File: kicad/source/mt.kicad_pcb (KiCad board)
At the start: 4 copper layers, 166.4 x 127 mm, 138 parts, among them IC1 MCP73831T-2ACI_OT, IC10 SN74HC148NSR, IC11 SN74HC148NSR, IC2 BQ29728DSER, IC3 TLV74333PDBVR, IC4 TLV9152IDR, IC5 MSPM0G3507SPMR, IC6 IS62WV1288BLL-55QLI, IC7 DAC082S085CIMMX_NOPB, IC8 SN74HC148NSR, IC9 SN74HC148NSR, J1 694106301002, J10 Conn_01x02_Pin, J2 3557-2, J3 SJ1-3524N, J4 Conn_01x05_Pin, J5 Conn_01x09_Pin, J6 Conn_01x03_Pin, J7 Conn_01x03_Pin, J8 Conn_01x03_Pin, J9 Conn_01x02_Pin, Q1 CSD16406Q3, Q2 CSD16406Q3, U1 1043

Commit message: completed buttons arrangement
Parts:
- moved R36 397.7 mm to (168.3, 142.9)
- moved S22 397.7 mm to (163.2, 148.0)
- moved R39 393.8 mm to (208.3, 101.0)
- moved S25 393.8 mm to (203.2, 106.0)
- moved R37 390.3 mm to (175.9, 131.4)
- moved S23 390.3 mm to (170.8, 136.5)
- moved R38 383.8 mm to (183.5, 142.9)
- moved S24 383.8 mm to (178.4, 148.0)
- moved R32 368.6 mm to (137.8, 142.9)
- moved S18 368.6 mm to (132.7, 148.0)
- moved R33 360.6 mm to (145.4, 131.4)
- moved S19 360.6 mm to (140.3, 136.5)
- moved C24 357.6 mm to (147.3, 88.3)
- moved IC10 357.6 mm to (141.6, 92.7)
- moved R34 354.7 mm to (153.0, 142.9)
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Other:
- board size 166.4 x 127 mm -> 166.4 x 142.2 mm
- board text added: "Cancel"
- board text added: "Copy"
- board text added: "Cut"
- board text added: "Delete"
- board text added: "Down"
- board text added: "Edit/Play"
- board text added: "Editor Config"
- board text added: "End"
- board text added: "Enter"
- board text added: "Keyboard"
- board text added: "Left"
- board text added: "Load"
- board text added: "Matthew Nutt - Rice University - ELEC 327"
- board text added: "MicroTracker"
- board text added: "Note End"
- board text added: "Octave +"
- board text added: "Octave -"
- board text added: "Pattern/Song"
- board text added: "Rev. 1.0"
- board text added: "Right"
- board text added: "Save"
- board text added: "Select"
- board text added: "Skip"
- board text added: "Song Config"
- board text added: "Undo"
- board text added: "Up"

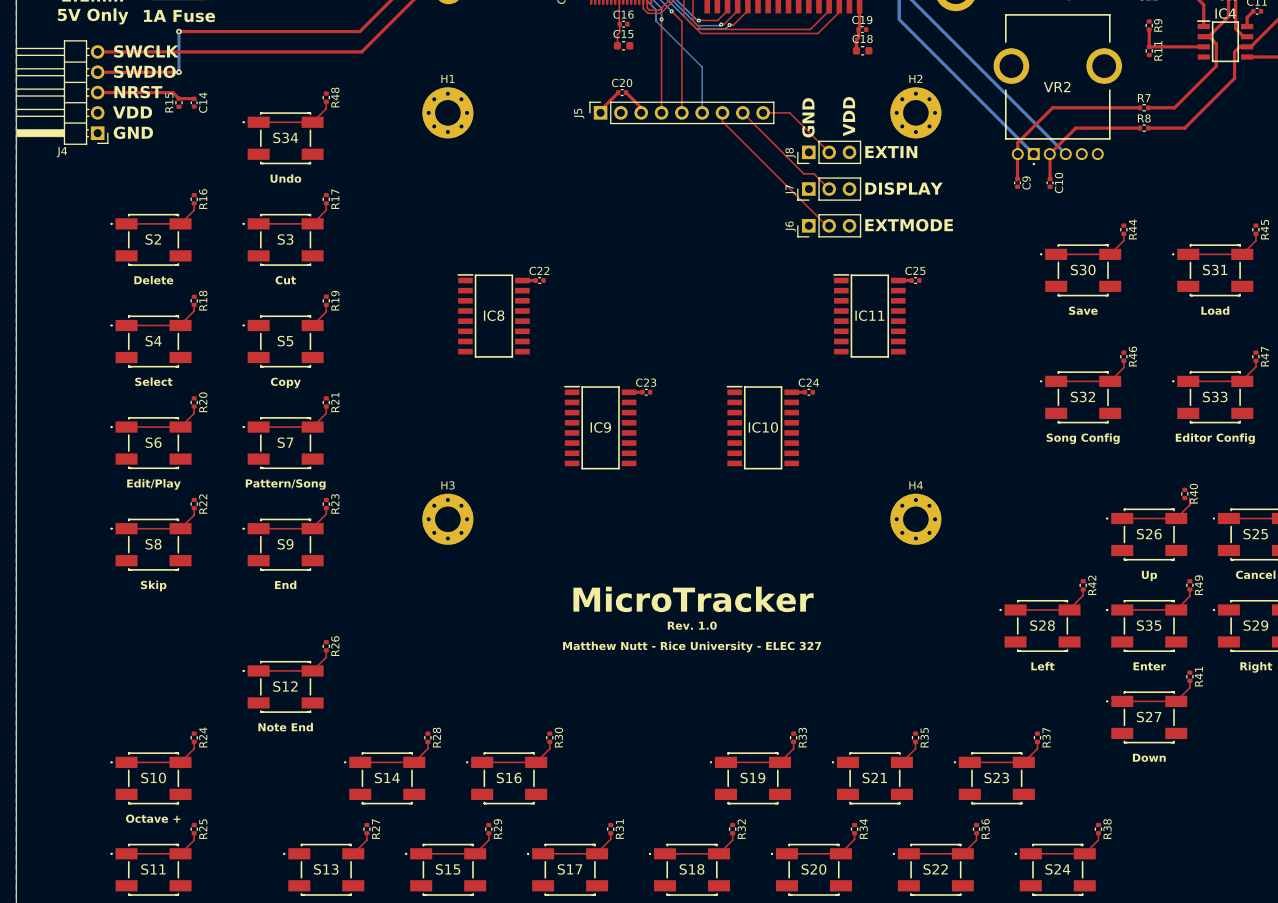
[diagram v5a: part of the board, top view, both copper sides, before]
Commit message: completed button-encoder routing
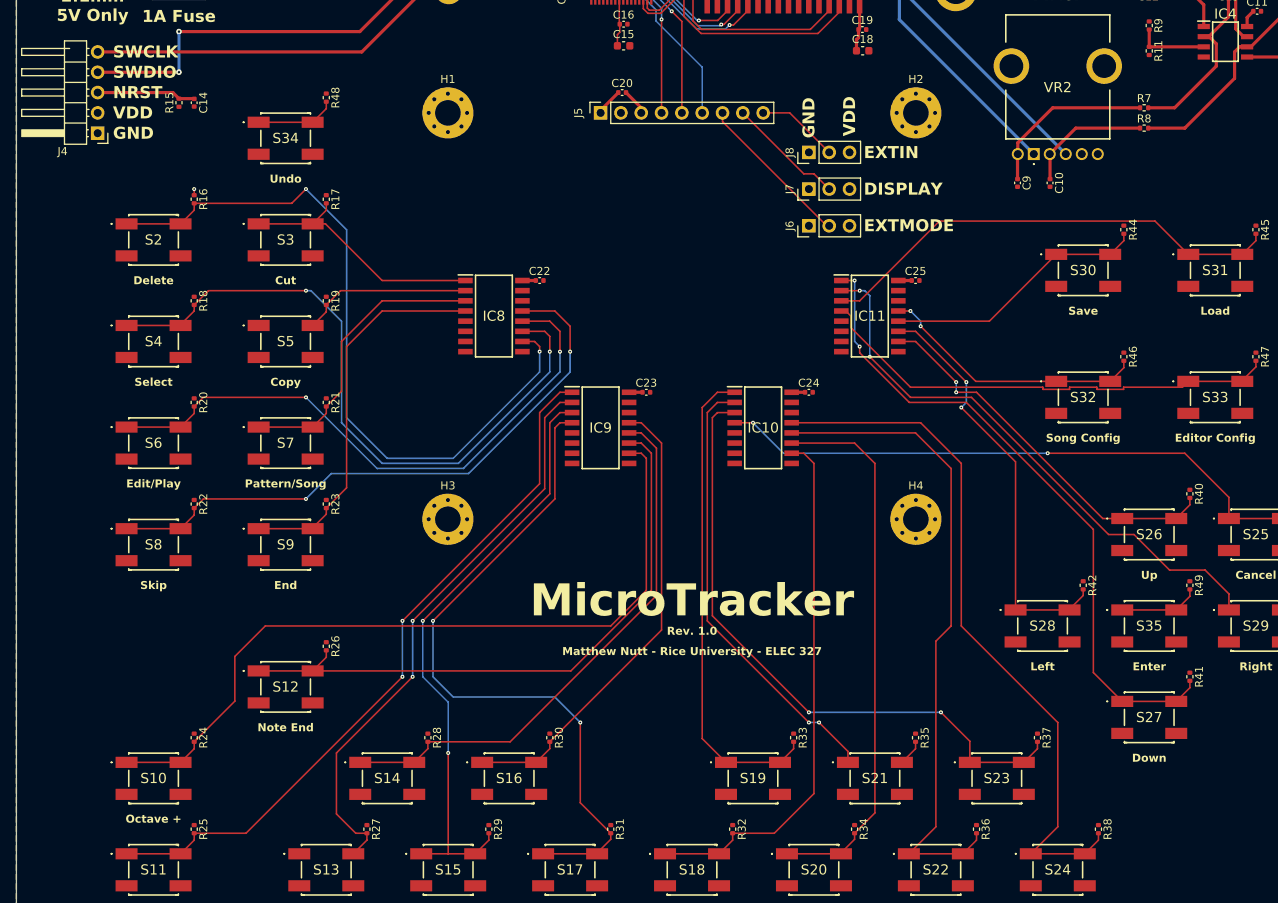
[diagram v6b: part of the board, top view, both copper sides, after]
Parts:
- moved R40 0.63 mm to (194.9, 101.0)
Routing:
- net Net-(IC9-0): track 10.0 -> 96.6 mm
- net Net-(IC8-0): track 10.0 -> 91.7 mm, vias 0 -> 2
- net Net-(IC9-4): track 10.0 -> 89.4 mm, vias 0 -> 2
- net Net-(IC10-3): track 10.0 -> 88.5 mm
- net Net-(IC9-7): track 10.0 -> 86.1 mm, vias 0 -> 2
- net Net-(IC8-1): track 10.0 -> 84.5 mm, vias 0 -> 2
- net Net-(IC11-4): track 10.0 -> 82.3 mm, vias 0 -> 2
- net Net-(IC10-2): track 10.0 -> 82.2 mm
- net Net-(IC11-5): track 3.28 -> 73.9 mm, vias 0 -> 2
- net Net-(IC9-5): track 3.28 -> 72.6 mm, vias 0 -> 2
- net Net-(IC10-6): track 10.0 -> 79.2 mm, vias 0 -> 2
- net Net-(IC10-7): track 10.0 -> 78.3 mm, vias 0 -> 2
- net Net-(IC9-1): track 10.0 -> 77.0 mm
- net Net-(IC8-3): track 10.0 -> 76.5 mm, vias 0 -> 2
- net Net-(IC8-2): track 10.0 -> 75.2 mm, vias 0 -> 2
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
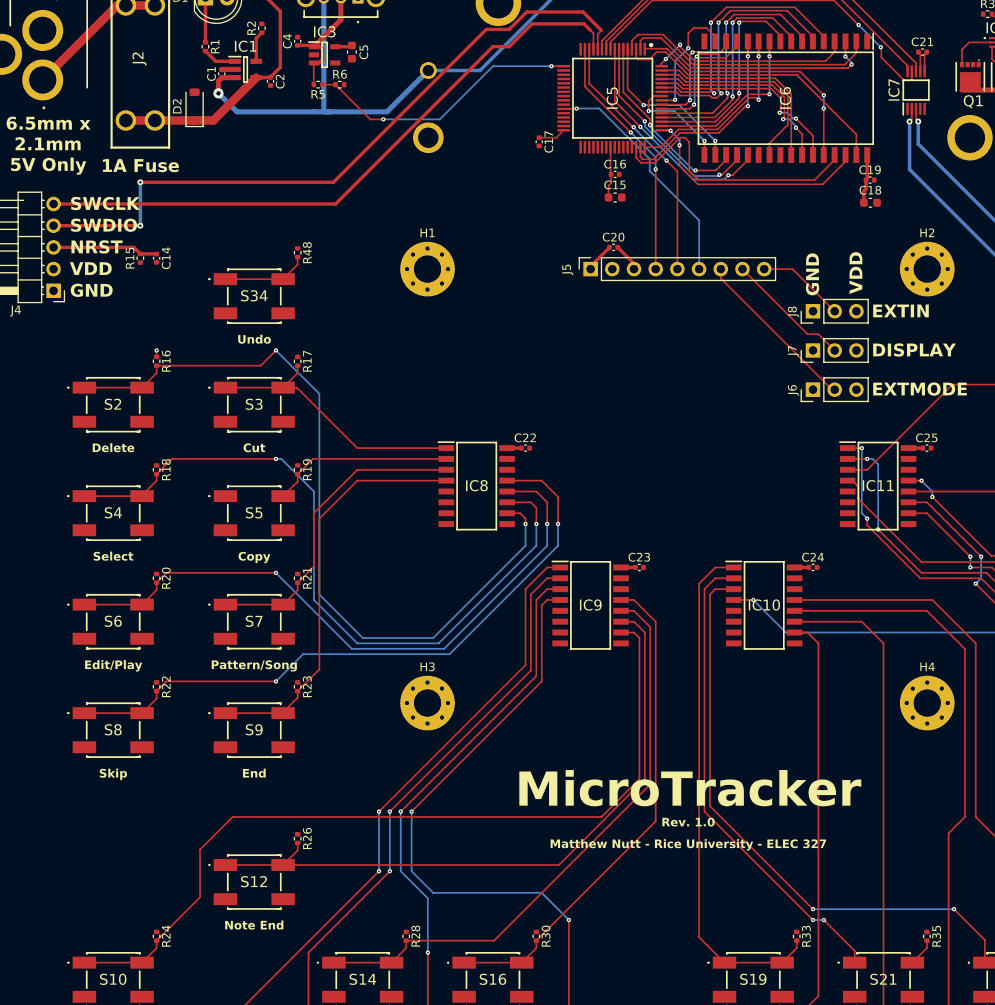
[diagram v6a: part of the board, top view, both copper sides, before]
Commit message: started encoder-microcontroller routing
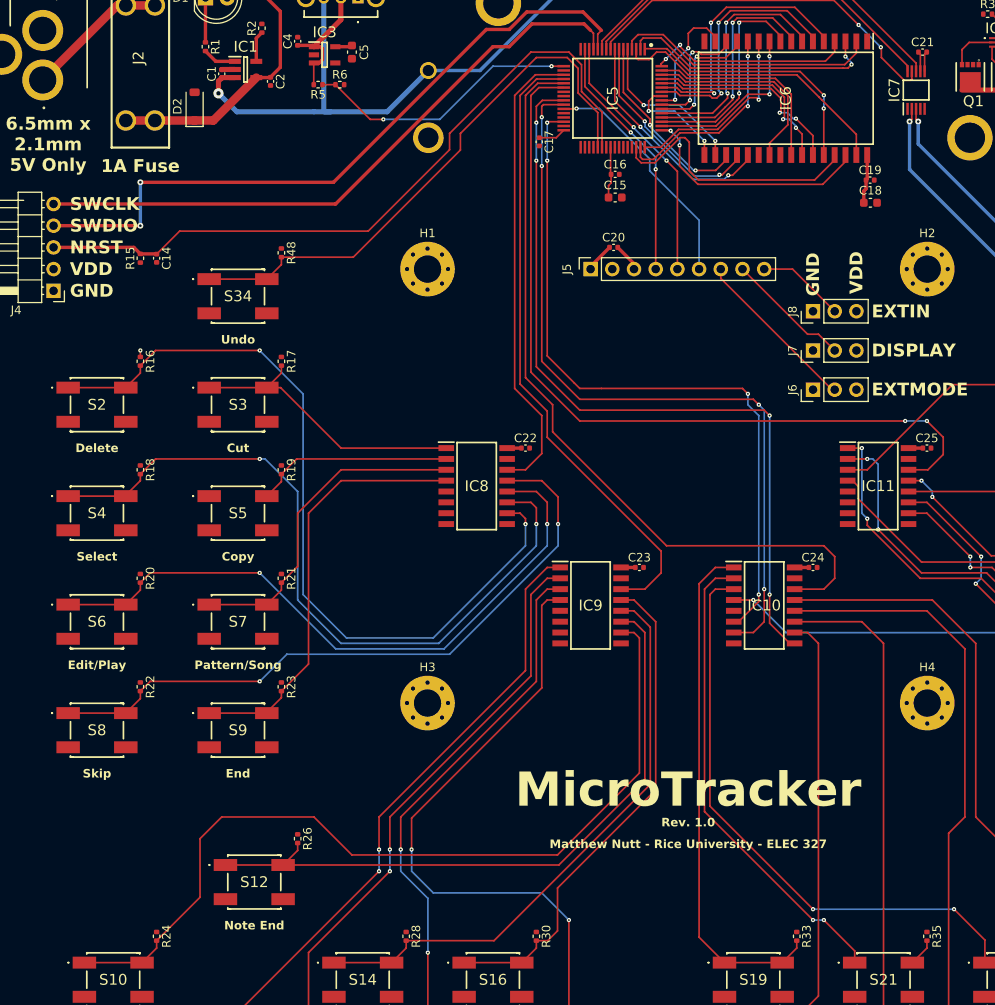
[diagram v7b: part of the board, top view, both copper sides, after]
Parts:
- moved R16 1.91 mm to (68.6, 64.1)
- moved R17 1.91 mm to (85.1, 64.1)
- moved R18 1.91 mm to (68.6, 76.8)
- moved R19 1.91 mm to (85.1, 76.8)
- moved R20 1.91 mm to (68.6, 89.5)
- moved R21 1.91 mm to (85.1, 89.5)
- moved R22 1.91 mm to (68.6, 102.2)
- moved R23 1.91 mm to (85.1, 102.2)
- moved R48 1.91 mm to (85.1, 51.4)
- moved S2 1.91 mm to (63.5, 69.2)
- moved S3 1.91 mm to (80.0, 69.2)
- moved S34 1.91 mm to (80.0, 56.5)
- moved S4 1.91 mm to (63.5, 81.9)
- moved S5 1.91 mm to (80.0, 81.9)
- moved S6 1.91 mm to (63.5, 94.6)
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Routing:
- net E3_GS: track 0.00 -> 94.8 mm, vias 0 -> 2
- net E2_GS: track 0.00 -> 92.6 mm
- net E2_0: track 0.00 -> 91.9 mm, vias 0 -> 4
- net E2_1: track 0.00 -> 89.7 mm, vias 0 -> 4
- net E2_2: track 0.00 -> 83.4 mm, vias 0 -> 4
- net E1_GS: track 0.00 -> 74.1 mm
- net NRST: track 12.3 -> 84.3 mm
- net Ex_0: track 10.0 -> 66.3 mm
- net E0_GS: track 0.00 -> 54.8 mm
- net Net-(IC9-0): track 96.6 -> 100.6 mm
- net Net-(IC8-6): track 36.5 -> 38.4 mm
- net Net-(IC8-5): track 21.4 -> 23.3 mm
- net Net-(IC8-4): track 32.1 -> 34.0 mm
- net Net-(IC8-3): track 76.5 -> 78.4 mm
- net Net-(IC8-2): track 75.2 -> 77.1 mm
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
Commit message: completed all routing
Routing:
- net Ex_1: track 10.0 -> 137.7 mm, vias 0 -> 2
- net E3_0: track 0.00 -> 83.1 mm, vias 0 -> 4
- net VDD: track 29.5 -> 112.1 mm, vias 1 -> 49
- net E3_1: track 0.00 -> 71.6 mm, vias 0 -> 2
- net E1_1: track 0.00 -> 68.8 mm, vias 0 -> 2
- net E1_0: track 0.00 -> 68.3 mm, vias 0 -> 4
- net E1_2: track 0.00 -> 61.2 mm, vias 0 -> 2
- net E3_2: track 0.00 -> 56.2 mm, vias 0 -> 2
- net E0_0: track 0.00 -> 51.4 mm, vias 0 -> 2
- net E0_2: track 0.00 -> 51.0 mm, vias 0 -> 2
- net E0_1: track 0.00 -> 50.9 mm, vias 0 -> 2
- net GND: track 11.0 -> 38.4 mm, vias 0 -> 14
- net Net-(IC10-5): track 59.0 -> 67.2 mm, vias 2 -> 4
- net Net-(IC9-5): track 72.6 -> 79.4 mm
- net Net-(IC8-5): track 23.3 -> 30.1 mm
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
